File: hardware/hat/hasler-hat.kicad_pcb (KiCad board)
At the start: 4 copper layers, 85 x 41 mm, 115 parts, among them J1 Amp4 top header, J2 Hasler J2, J3 USB-C PD in, J4 Debug / expansion, J5 Qwiic, J6 To Amp4 DC in, Q1 AO4407A, Q2 2N7002, U1 MCP23017, U10 SRV05-4, U11 SRV05-4, U12 SRV05-4, U2 ADS1115, U3 CH224A, U4 LM393, U5 AZ431AN, U6 XC6206P332MR, U7 SRV05-4, U8 SRV05-4, U9 SRV05-4

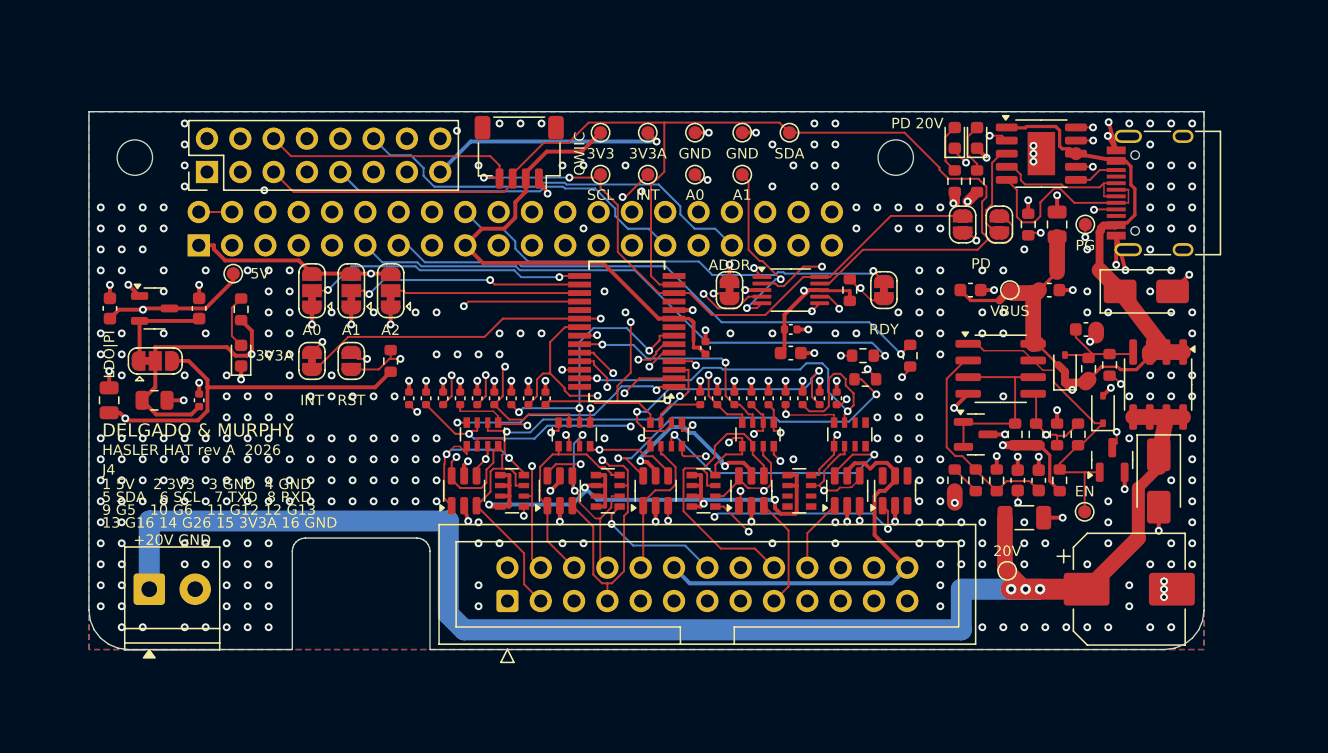
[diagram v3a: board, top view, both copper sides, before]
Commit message: HAT: review fixes - notch over the standing cap, soft start, VBUS strap, keepouts, thermals, silkscreen
From the five-reviewer pass:
- notch moved to x 11.5-22.5 (HAT coords): the Amp4's 8 mm cap stands over
  leads at x 15.13/18.93; the old notch came from the lying-down model
- turn-on: C6 470 nF (Miller, ~1.4-3.5 A inrush instead of 7-16 A),
  C17 10 uF gate-source (a fast VBUS edge can't turn the FET on), C18 1 uF on
  EN (waits out the PD transition)
- R13 (ADS RDY pull-up) to the Pi's 3V3; 100 nF at every SRV05-4 VCC
- J3's VBUS pad pairs joined by a bottom-layer strap under the pad row;
  CH224A VHV-VBUS, CC1 and D+ laid through vias before routing
- no tracks/vias within 3 mm of the mounting holes; thermal spokes on THT GND
- silkscreen >= 1.0 mm text, >= 0.15 mm lines; J2 pin 1 marked inboard
- build.sh stops on DRC errors; gap-closer and width passes reworked
- ORDERING.md: J1 hand-soldered, review options, bring-up checks; DESIGN.md

DRC 0 / 0 unconnected / parity clean, ERC 0.

Co-Authored-By: Claude Opus 5.5 <noreply@anthropic.com>
Claude-Session: https://claude.ai/code/session_014wovV18Ypx4LXt9k8BSCRk
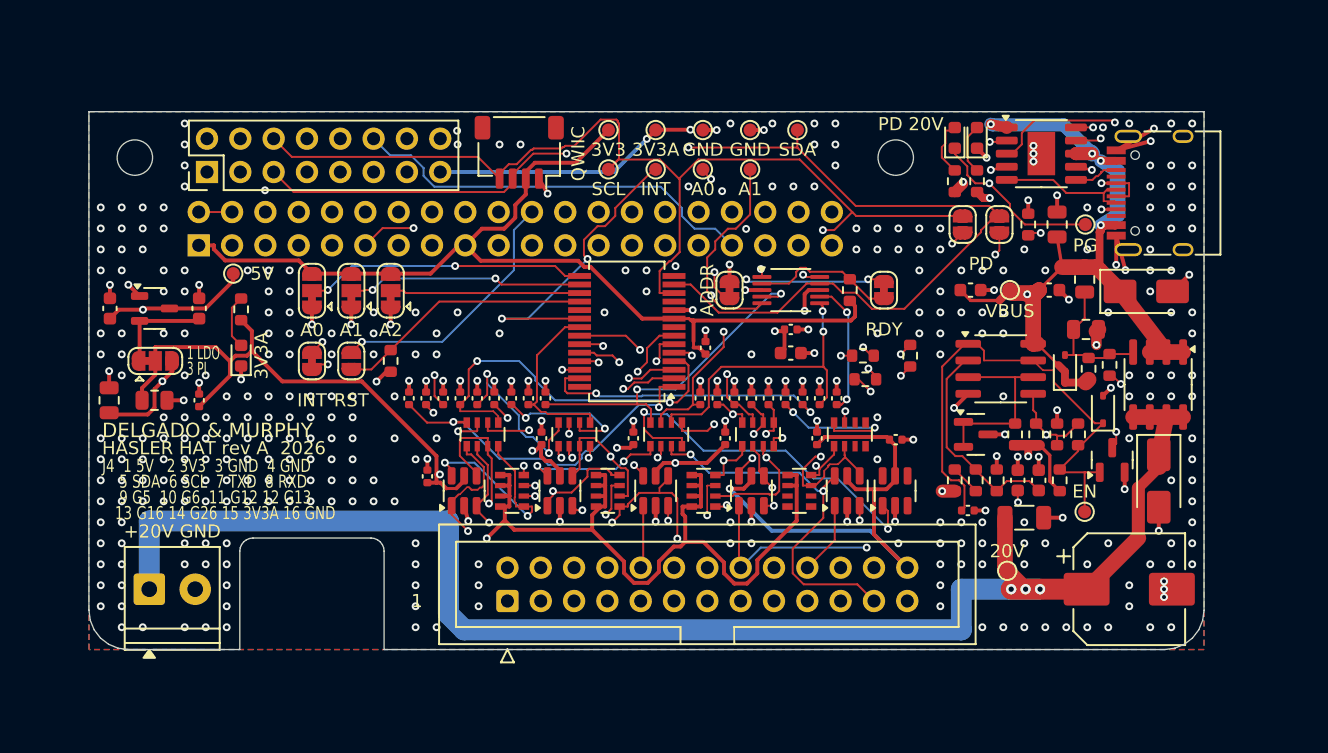
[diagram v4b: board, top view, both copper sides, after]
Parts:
- added C17: 10uF, Capacitor_SMD:C_0805_2012Metric, F.Cu at (175.9, 112.8)
- added C18: 1uF, Capacitor_SMD:C_0402_1005Metric, F.Cu at (167.0, 130.4)
- added C38: 100nF, Capacitor_SMD:C_0402_1005Metric, F.Cu at (125.8, 127.8)
- added C39: 100nF, Capacitor_SMD:C_0402_1005Metric, F.Cu at (134.5, 124.9)
- added C40: 100nF, Capacitor_SMD:C_0402_1005Metric, F.Cu at (141.5, 124.9)
- added C41: 100nF, Capacitor_SMD:C_0402_1005Metric, F.Cu at (148.5, 124.9)
- added C42: 100nF, Capacitor_SMD:C_0402_1005Metric, F.Cu at (155.5, 124.9)
- added C43: 100nF, Capacitor_SMD:C_0402_1005Metric, F.Cu at (161.5, 125.0)
- C6: value 100nF -> 470nF; footprint Capacitor_SMD:C_0603_1608Metric -> Capacitor_SMD:C_0805_2012Metric
- moved TP13 0.72 mm to (146.8, 104.4)
- moved TP10 0.72 mm to (143.2, 104.4)
- moved TP14 0.72 mm to (150.4, 104.4)
- moved TP9 0.72 mm to (139.6, 104.4)
- moved TP6 0.63 mm to (146.8, 101.4)
- moved TP4 0.63 mm to (139.6, 101.4)
- moved TP5 0.63 mm to (143.2, 101.4)
- moved TP7 0.63 mm to (150.4, 101.4)
- moved TP8 0.63 mm to (154.0, 101.4)
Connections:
- R13 pad 1: /3V3A -> /+3V3
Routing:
- net /PD_SDA: track 7.52 -> 37.1 mm, vias 0 -> 2
- net /SCL: track 76.3 -> 92.0 mm
- net /3V3A: track 188.2 -> 203.7 mm, vias 7 -> 9
- net /EN: track 24.5 -> 39.8 mm
- net /J_TSW: track 35.6 -> 21.1 mm, vias 2 -> 3
- net /+3V3: track 184.7 -> 196.9 mm, vias 6 -> 3
- net /J_LR: track 36.4 -> 46.2 mm
- net /J_X1: track 28.8 -> 19.8 mm, vias 1 -> 2
- net /M_X5: track 25.1 -> 33.7 mm, vias 2 -> 3
- net /GND: track 72.4 -> 81.0 mm, vias 396 -> 369
- net /M_A3: track 33.1 -> 24.8 mm
- net /M_K5: track 24.3 -> 32.5 mm
- net /M_X6: track 33.6 -> 25.9 mm, vias 2 -> 3
- net /J_K6: track 25.5 -> 18.3 mm, vias 2 -> 3
- net /J_X4: track 21.8 -> 28.7 mm
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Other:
- outline, holes or cut-outs redrawn
- board text added: "+ to +. Amp4 DC jack"
- board text added: "1"
- board text added: "1 K1 / key1"
- board text added: "1 LDO"
- board text added: "12 3V3A pots,LED+"
- board text added: "14 tone sw/key0"
- board text added: "25 spare A3"
- board text added: "3 K2 / key2"
- board text added: "3 PI"
- board text added: "4 K3 / key3"
- board text added: "5 K4 / key4"
- board text added: "6 K5 / key5"
- board text added: "7 K6 / key6"
- board text added: "9 tone/treble"
- board text added: "ADS1115 0x48"
- board text added: "AMP 0x4D"
- board text added: "CH224A 0x22 JP9/10"
- board text added: "J2 IDC: wire 1 = pin 1"
- board text added: "J4 1 5V 2 3V3 3 GND 4 GND"
- board text added: "J6 -> Amp4 power in,"
- board text added: "Never 28 V (R1 120k)."
- board text added: "Window 10.8-22.8 V."
- board text added: "stays empty."
- board text removed: "+ to +. Leave the Amp4 DC"
- board text removed: "1 5V 2 3V3 3 GND 4 GND"
- board text removed: "1 K1 / key 1"
- board text removed: "12 3V3A (pots, LED +)"
- board text removed: "14 tone sw / key 0"
- board text removed: "25 spare analog"
- board text removed: "3 K2 / key 2"
- board text removed: "4 K3 / key 3"
- board text removed: "5 K4 / key 4"
- board text removed: "6 K5 / key 5"
- board text removed: "7 K6 / key 6"
- board text removed: "9 tone / treble"
- board text removed: "ADS1115 0x48 AMP 0x4D"
- board text removed: "CH224A 0x22 (JP9/JP10)"
- board text removed: "J2 (IDC) wire 1 = pin 1"
- board text removed: "J4"
- board text removed: "J6 -> Amp4 Pro power terminal,"
- board text removed: "LDO|PI"
- board text removed: "Never set the CH224A to 28 V."
- board text removed: "Window passes 10.8-22.8 V."
- board text removed: "jack empty."

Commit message: HAT: TPS259474A eFuse replaces the discrete window + P-FET; second VBUS path; routing fixes
Second review round: the discrete soft start (C6 470 nF + C17 10 uF) made the
inrush scale with the Amp4's unknown input capacitance and slowed OV turn-off to
~50 ms. U4 is now a TI TPS259474A (C3662807): UVLO 11.2 V, OVLO 23.0 V in 1.2 us,
dV/dt 0.9 V/ms (0.9 A into 1000 uF), 3.3 A circuit breaker with 18 ms blanking,
true reverse-current blocking, PG to TP12. Footprint hasler:TI_RPW0010A built
from TI's land pattern (no KiCad library part).

Also: a second B.Cu path from J3's VBUS strap to D1; LEDs turned to face their
resistors; CH224A I2C stubs and the MCP-ADS SDA link laid before routing; the
gap-closer gains a two-via fallback and stops when it stalls. DRC 0/0, ERC 0.

Co-Authored-By: Claude Opus 5.5 <noreply@anthropic.com>
Claude-Session: https://claude.ai/code/session_014wovV18Ypx4LXt9k8BSCRk
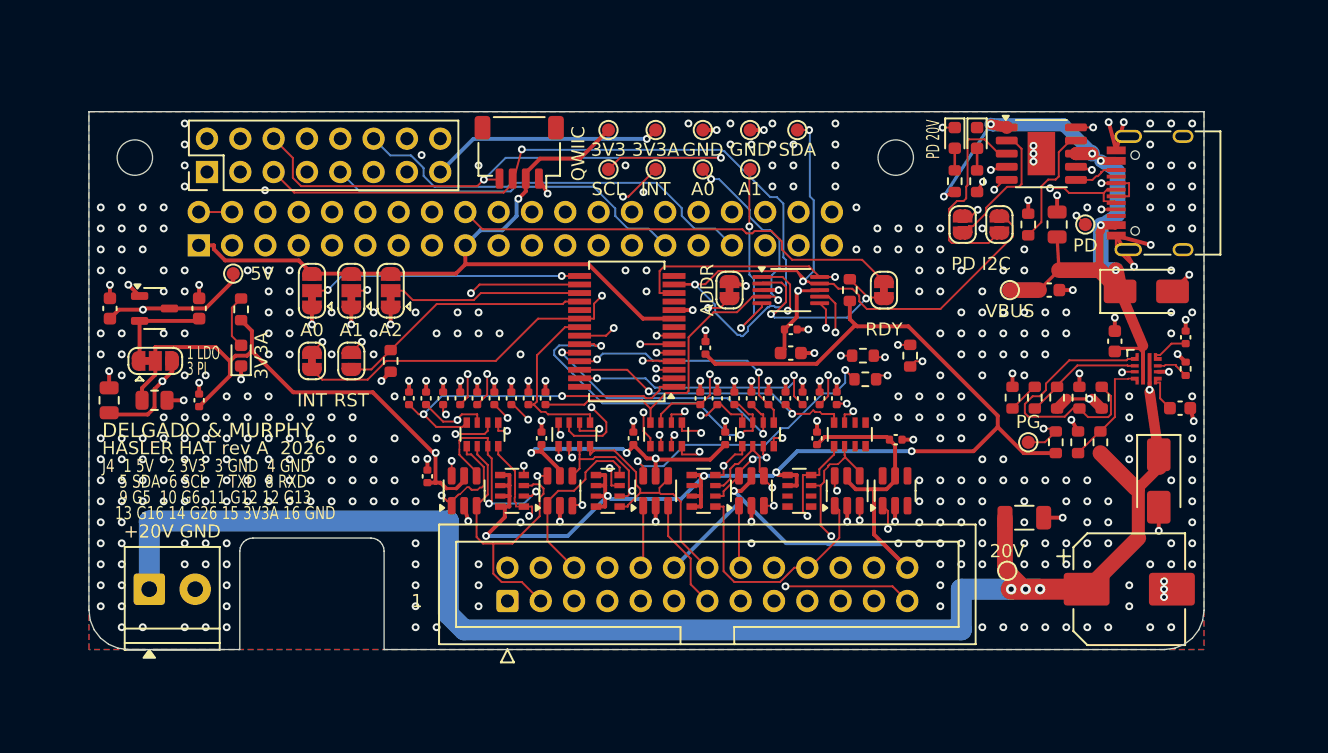
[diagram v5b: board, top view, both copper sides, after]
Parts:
- removed C17: 10uF, Capacitor_SMD:C_0805_2012Metric
- removed C18: 1uF, Capacitor_SMD:C_0402_1005Metric
- removed C6: 470nF, Capacitor_SMD:C_0805_2012Metric
- removed D3, D4: BZT52C15S, Diode_SMD:D_SOD-323
- removed Q1: AO4407A, Package_SO:SOIC-8_3.9x4.9mm_P1.27mm
- removed Q2: 2N7002, Package_TO_SOT_SMD:SOT-23
- removed R16: 1M, Resistor_SMD:R_0603_1608Metric
- removed U5: AZ431AN, Package_TO_SOT_SMD:SOT-23
- C3: value 1nF -> 2.2nF
- C4: value 1nF -> 22nF; footprint Capacitor_SMD:C_0603_1608Metric -> Capacitor_SMD:C_0402_1005Metric
- C5: value 100nF -> 1uF
- R14: value 10k -> 1k; footprint Resistor_SMD:R_0603_1608Metric -> Resistor_SMD:R_0402_1005Metric
- R15: value 4.7k -> 10k
- R3: value 6.8k -> 1M
- R4: value 33k -> 120k
- R5: value 33k -> 2M
- R6: value 5.1k -> 100k
- R7: value 100k -> 10k
- R8: value 2.2k -> 1M
- R9: value 4.7k -> 120k
- TP11: value PG -> PD
- TP12: value EN -> PG
- U4: value LM393 -> TPS259474ARPWR; footprint Package_SO:SOIC-8_3.9x4.9mm_P1.27mm -> hasler:TI_RPW0010A_VQFN-HR-10_2x2mm_P0.45mm
- moved C4 15.6 mm to (183.6, 117.2)
- moved C3 13.5 mm to (183.2, 122.6), turned to 0 degrees
- moved C5 11.7 mm to (178.2, 117.5), turned to 90 degrees
- moved U4 11.1 mm to (180.6, 119.6)
- moved R14 11.0 mm to (183.6, 119.6)
- moved R5 10.0 mm to (173.8, 121.8)
- moved R6 7.74 mm to (172.1, 121.8)
- moved R7 7.26 mm to (170.4, 121.8)
- moved R3 7.17 mm to (177.2, 121.8)
- moved TP12 6.82 mm to (171.6, 125.2)
- moved R8 5.94 mm to (177.1, 125.2)
- moved R9 5.66 mm to (175.4, 125.2)
- moved R15 5.35 mm to (173.7, 125.2)
- moved R4 4.33 mm to (175.5, 121.8)
- turned D2 to -90 degrees
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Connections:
- C3 pad 1: /DIV_UV -> /EF_DVDT
- C4 pad 1: /DIV_OV -> /EF_TMR
- R14 pad 1: /DIV_UV -> /EF_ILM
- R15 pad 1: /DIV_OV -> /+3V3
- R15 pad 2: /GND -> /EF_PG
- R3 pad 2: /VREF -> /EF_EN
- R4 pad 1: /VBUS -> /EF_EN
- R4 pad 2: /DIV_UV -> /GND
- R5 pad 2: /DIV_OVT -> /EF_OV
- R6 pad 1: /DIV_OVT -> /EF_OV
- R6 pad 2: /DIV_OV -> /EF_OVB
- R7 pad 1: /VBUS -> /EF_OVB
- R7 pad 2: /EN -> /GND
- R8 pad 1: /GATE_PULL -> /VOUT
- R8 pad 2: /PGATE -> /EF_PGTH
- R9 pad 1: /VBUS -> /EF_PGTH
- R9 pad 2: /PGATE -> /GND
- TP12 pad 1: /EN -> /EF_PG
- U4 pad 1: /EN -> /EF_EN
- U4 pad 2: /DIV_OV -> /EF_OV
- U4 pad 3: /VREF -> /EF_PG
- U4 pad 4: /GND -> /EF_PGTH
- U4 pad 5: /DIV_UV -> /VBUS
- U4 pad 6: /VREF -> /VOUT
- U4 pad 7: /EN -> /EF_DVDT
- U4 pad 8: /VBUS -> /GND
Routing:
- net /EN: track 39.8 -> 0.00 mm
- net /VBUS: track 97.8 -> 76.8 mm, vias 8 -> 7
- net /PD_SDA: track 37.1 -> 16.2 mm, vias 2 -> 0
- net /EF_EN: track 0.00 -> 20.9 mm
- net /+3V3: track 196.9 -> 217.4 mm, vias 3 -> 8
- net /SDA: track 102.3 -> 119.9 mm, vias 2 -> 4
- net /DIV_OV: track 16.5 -> 0.00 mm
- net /VREF: track 14.3 -> 0.00 mm
- net /DIV_UV: track 14.1 -> 0.00 mm, vias 2 -> 0
- net /J_A2: track 29.2 -> 42.7 mm
- net /EF_PG: track 0.00 -> 12.4 mm, vias 0 -> 2
- net /M_X5: track 33.7 -> 22.6 mm, vias 3 -> 2
- net /PGATE: track 10.6 -> 0.00 mm
- net /SCL: track 92.0 -> 101.6 mm, vias 2 -> 4
- net /J_LR: track 46.2 -> 36.6 mm, vias 2 -> 1
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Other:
- board text added: "PD I2C"
- board text added: "eFuse 11.2-23 V 3.3 A"
- board text removed: "EN"
- board text removed: "Window 10.8-22.8 V."

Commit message: HAT: eFuse review fixes - thresholds for tolerance, C7 not fitted, IN/OUT ceramics and heat copper
Third review round (eFuse circuit + layout/fab):
- UVLO 10.3 V (R4 120k + R16 12k): a 12 V -5 % contract starts in the worst
  case; OVLO 22.6 V (R7 12k): 21.7-23.7 V worst case, under the amp's 24 V
- C7 (220 uF) not fitted: the eFuse has no power limit at start-up, so VOUT
  capacitance sets its heating; the Amp4 has its own input cap
- C17 1 uF on the OUT run, C5 moved onto the IN run, small VBUS/VOUT pours on
  F/B.Cu with vias round U4 (no exposed pad: the strips are the heat path)
- footprint to TI's exact land pattern (gen/make_fp.py), 82 % paste on IN/OUT
- second vias on the VBUS strap and D1 path; C41/C42 short to their ESD arrays
- R15 100k; docs: start-up check, barrel-jack limit, counts; hardware.md note

DRC 0/0, ERC 0. BOM 35 lines / 89 placements.

Co-Authored-By: Claude Opus 5.5 <noreply@anthropic.com>
Claude-Session: https://claude.ai/code/session_014wovV18Ypx4LXt9k8BSCRk
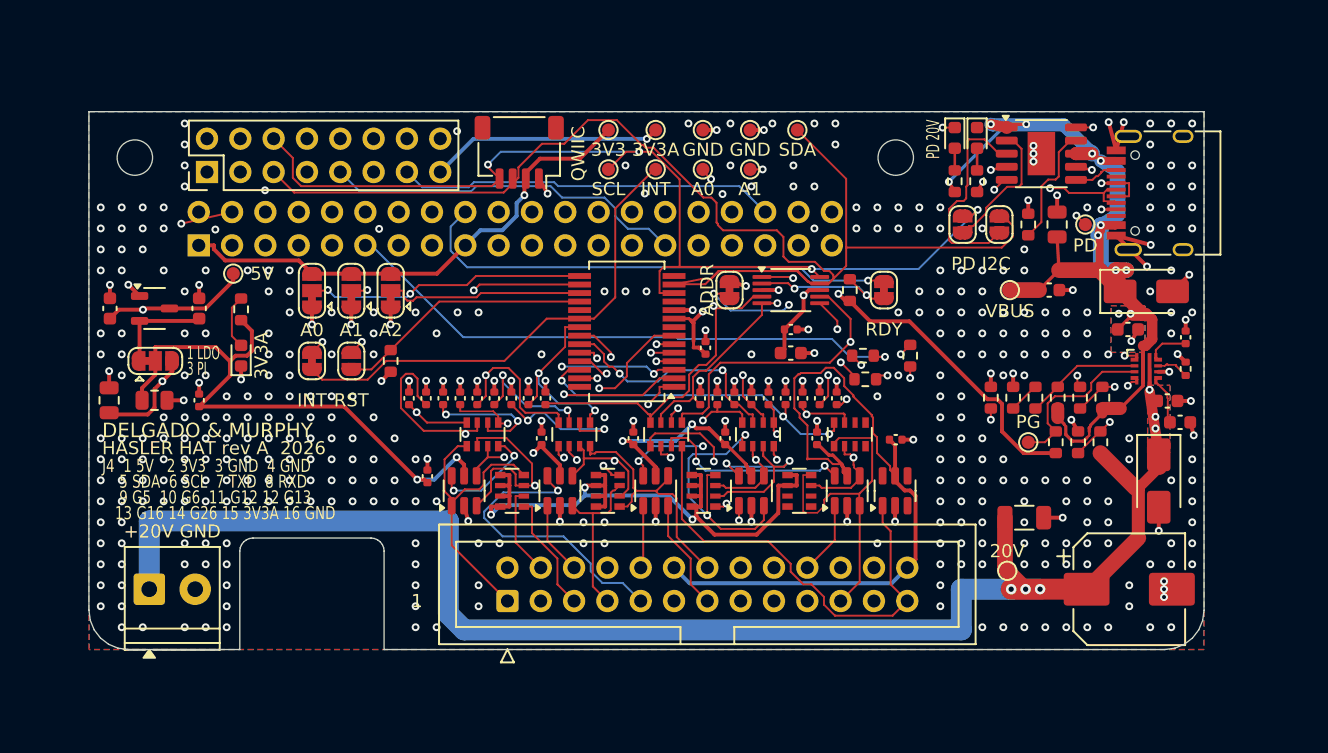
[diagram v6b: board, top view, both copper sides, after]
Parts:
- added C17: 1uF, Capacitor_SMD:C_0603_1608Metric, F.Cu at (182.2, 122.0)
- added R16: 12k, Resistor_SMD:R_0603_1608Metric, F.Cu at (168.8, 121.8)
- R15: value 10k -> 100k
- R7: value 10k -> 12k
- moved C5 1.35 mm to (179.2, 116.6), turned to 0 degrees
- moved C3 1.08 mm to (183.2, 123.7)
- moved R3 0.05 mm to (177.2, 121.8)
- moved R4 0.05 mm to (175.6, 121.8)
- moved R6 0.05 mm to (172.2, 121.8)
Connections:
- R4 pad 2: /GND -> /EF_ENB
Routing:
- net /3V3A: track 198.5 -> 225.0 mm
- net /J_A0: track 28.2 -> 44.4 mm
- net /J_A2: track 42.7 -> 27.1 mm
- net /SCL: track 101.6 -> 87.3 mm
- net /EF_EN: track 20.9 -> 7.31 mm, vias 0 -> 2
- net /J_X1: track 19.9 -> 31.7 mm
- net /EF_ENB: track 0.00 -> 9.79 mm, vias 0 -> 2
- net /J_X3: track 18.9 -> 27.9 mm
- net /M_X2: track 26.6 -> 18.1 mm
- net /M_PU: track 20.5 -> 28.6 mm
- net /J_K6: track 17.9 -> 25.6 mm, vias 3 -> 1
- net /J_X4: track 30.7 -> 23.6 mm, vias 1 -> 2
- net /+3V3: track 217.4 -> 210.7 mm
- net /VOUT: track 150.6 -> 144.1 mm, vias 5 -> 7
- net /GPIO16: track 35.2 -> 28.9 mm
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- added copper zone on B.Cu, net /VBUS
- added copper zone on F.Cu, net /VBUS
- added copper zone on B.Cu, net /VOUT
- added copper zone on F.Cu, net /VOUT
